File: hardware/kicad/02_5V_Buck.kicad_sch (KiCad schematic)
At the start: 9 parts, among them U101 LMR36520ADDAR 5V/2A CANDIDATE

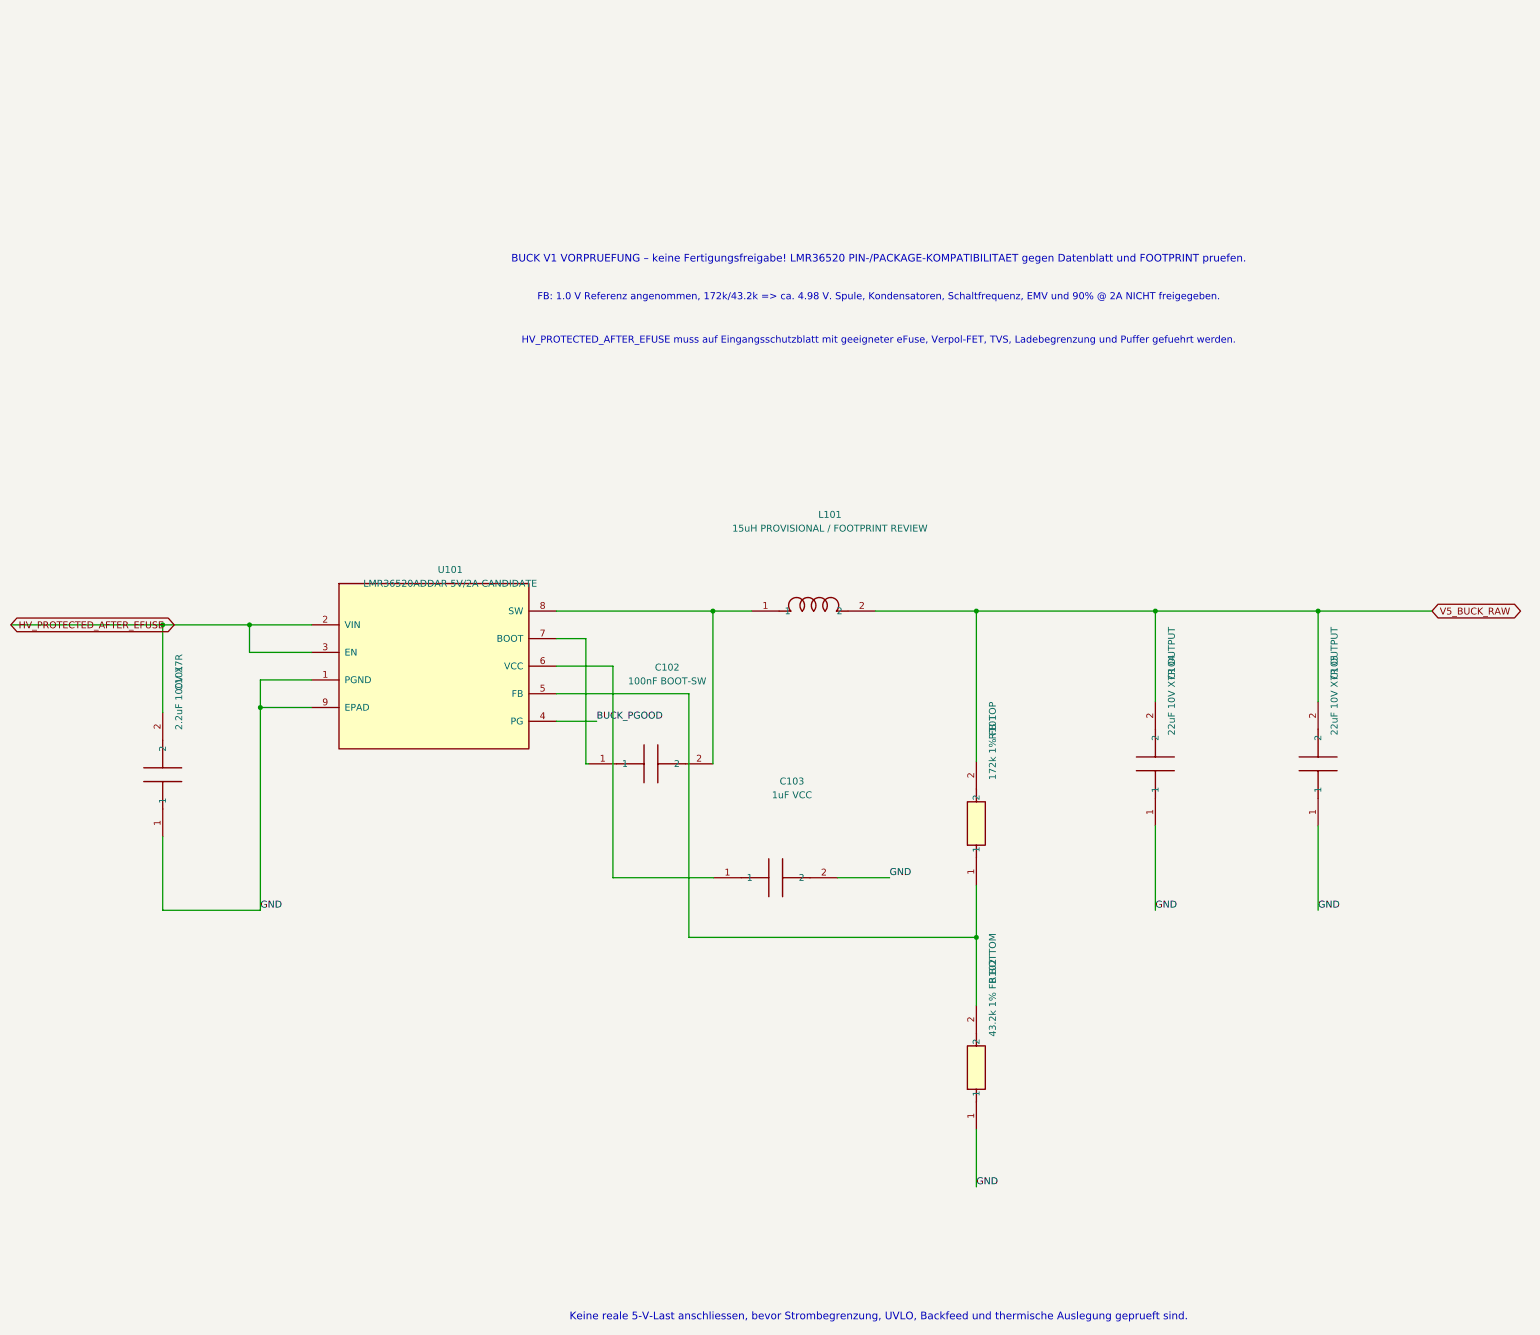
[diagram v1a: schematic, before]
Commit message: kicad: update 5V buck TI Rev C passives, 5A inductor candidate, isolate ENABLE from VIN
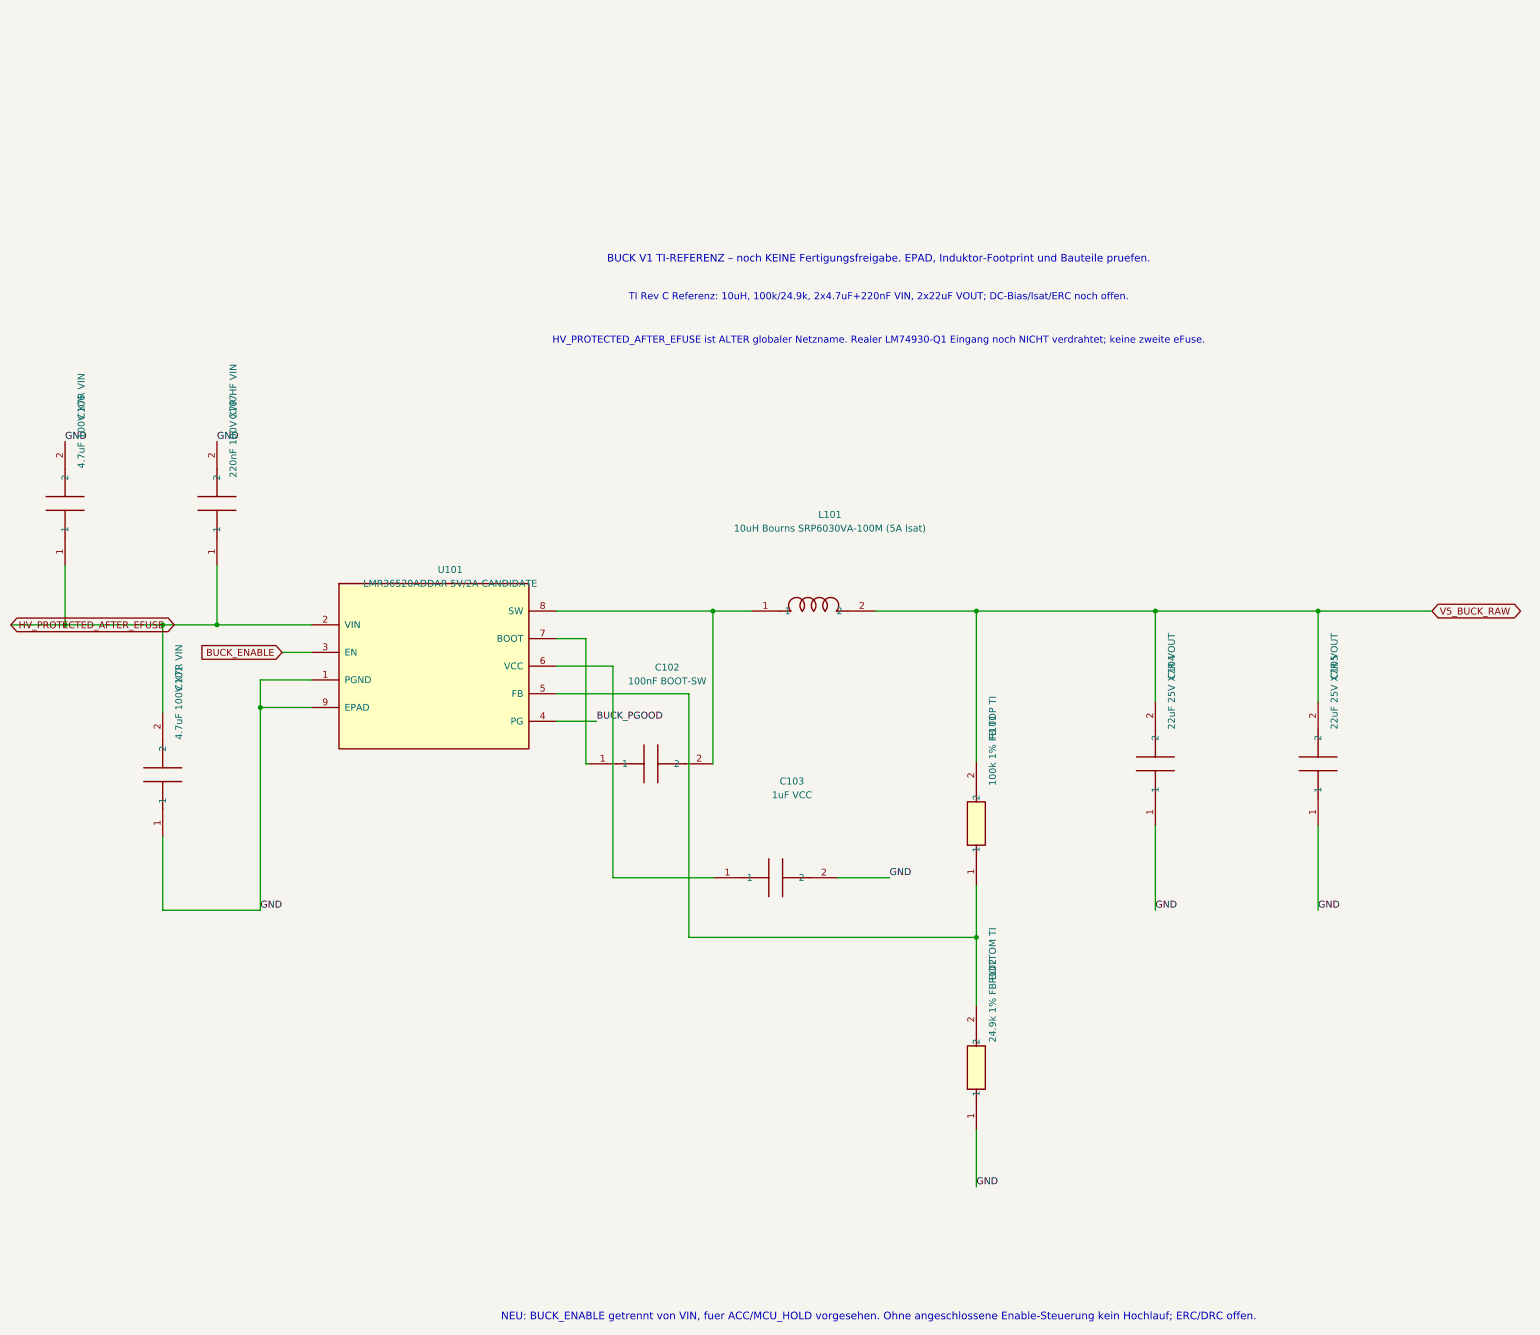
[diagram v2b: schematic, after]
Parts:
- added C106: 4.7uF 100V X7R VIN, Tripmaster:C_1210_3225, symbol Tripmaster_Sym:C1210
- added C107: 220nF 100V X7R HF VIN, Tripmaster:C_1206_3216, symbol Tripmaster_Sym:C
- C101: value 2.2uF 100V X7R -> 4.7uF 100V X7R VIN
- C104, C105: value 22uF 10V X7R OUTPUT -> 22uF 25V X7R VOUT
- L101: value 15uH PROVISIONAL / FOOTPRINT REVIEW -> 10uH Bourns SRP6030VA-100M (5A Isat); footprint Tripmaster:L1_Bourns_SRN6045_220M -> (none)
- R101: value 172k 1% FB TOP -> 100k 1% FB TOP TI
- R102: value 43.2k 1% FB BOTTOM -> 24.9k 1% FB BOTTOM TI
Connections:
- net GND: now also C106.2, C107.2
- net HV_PROTECTED_AFTER_EFUSE: now also C106.1, C107.1; no longer U101.3 (EN)
- new net BUCK_ENABLE: U101.3 (EN)
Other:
- note added: "BUCK V1 TI-REFERENZ – noch KEINE Fertigungsfreigabe. EPAD, Induktor-Footprint und Bauteile pruefen."
- note added: "HV_PROTECTED_AFTER_EFUSE ist ALTER globaler Netzname. Realer LM74930-Q1 Eingang noch NICHT verdrahtet; keine zweite eFuse."
- note added: "NEU: BUCK_ENABLE getrennt von VIN, fuer ACC/MCU_HOLD vorgesehen. Ohne angeschlossene Enable-Steuerung kein Hochlauf; ERC/DRC offen."
- note added: "TI Rev C Referenz: 10uH, 100k/24.9k, 2x4.7uF+220nF VIN, 2x22uF VOUT; DC-Bias/Isat/ERC noch offen."
- note removed: "BUCK V1 VORPRUEFUNG – keine Fertigungsfreigabe! LMR36520 PIN-/PACKAGE-KOMPATIBILITAET gegen Datenblatt und FOOTPRINT pruefen."
- note removed: "FB: 1.0 V Referenz angenommen, 172k/43.2k => ca. 4.98 V. Spule, Kondensatoren, Schaltfrequenz, EMV und 90% @ 2A NICHT freigegeben."
- note removed: "HV_PROTECTED_AFTER_EFUSE muss auf Eingangsschutzblatt mit geeigneter eFuse, Verpol-FET, TVS, Ladebegrenzung und Puffer gefuehrt werden."
- note removed: "Keine reale 5-V-Last anschliessen, bevor Strombegrenzung, UVLO, Backfeed und thermische Auslegung geprueft sind."
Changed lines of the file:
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@@
 (kicad_sch (version 20250114) (generator "eeschema")
- (paper "A3") (title_block (title "TripTracer V1 – 5 V Buck: ELEKTRISCHER ENTWURF") (date "2026-10-13") (rev "a0 / ERC NICHT GEPRUEFT"))
- (text "BUCK V1 VORPRUEFUNG – keine Fertigungsfreigabe! LMR36520 PIN-/PACKAGE-KOMPATIBILITAET gegen Datenblatt und FOOTPRINT pruefen." (at 200 25 0) (effects (font (size 1.4 1.4))))
- (text "FB: 1.0 V Referenz angenommen, 172k/43.2k => ca. 4.98 V. Spule, Kondensatoren, Schaltfrequenz, EMV und 90% @ 2A NICHT freigegeben." (at 200 32 0) (effects (font (size 1.3 1.3))))
- (text "HV_PROTECTED_AFTER_EFUSE muss auf Eingangsschutzblatt mit geeigneter eFuse, Verpol-FET, TVS, Ladebegrenzung und Puffer gefuehrt werden." (at 200 40 0) (effects (font (size 1.3 1.3))))
- (text "Keine reale 5-V-Last anschliessen, bevor Strombegrenzung, UVLO, Backfeed und thermische Auslegung geprueft sind." (at 200 220 0) (effects (font (size 1.4 1.4))))
+ (paper "A3") (title_block (title "TripTracer V1 – 5 V Buck: ELEKTRISCHER ENTWURF") (date "2026-10-13") (rev "a1 / TI-REF 5V 2A / ERC OFFEN"))
+ (text "BUCK V1 TI-REFERENZ – noch KEINE Fertigungsfreigabe. EPAD, Induktor-Footprint und Bauteile pruefen." (at 200 25 0) (effects (font (size 1.4 1.4))))
+ (text "TI Rev C Referenz: 10uH, 100k/24.9k, 2x4.7uF+220nF VIN, 2x22uF VOUT; DC-Bias/Isat/ERC noch offen." (at 200 32 0) (effects (font (size 1.3 1.3))))
+ (text "HV_PROTECTED_AFTER_EFUSE ist ALTER globaler Netzname. Realer LM74930-Q1 Eingang noch NICHT verdrahtet; keine zweite eFuse." (at 200 40 0) (effects (font (size 1.3 1.3))))
+ (text "NEU: BUCK_ENABLE getrennt von VIN, fuer ACC/MCU_HOLD vorgesehen. Ohne angeschlossene Enable-Steuerung kein Hochlauf; ERC/DRC offen." (at 200 220 0) (effects (font (size 1.4 1.4))))
  (symbol (lib_id "TripTracer_V1:LMR36520") (at 118 100 0) (unit 1) (exclude_from_sim no) (in_bom yes) (on_board yes) (dnp no)
  (property "Reference" "U101" (at 121 82.22 0) (effects (font (size 1.27 1.27))))
@@
 (symbol (lib_id "Tripmaster_Sym:L") (at 188 89.84 0) (unit 1) (exclude_from_sim no) (in_bom yes) (on_board yes) (dnp no)
  (property "Reference" "L101" (at 191 72.06 0) (effects (font (size 1.27 1.27))))
- (property "Value" "15uH PROVISIONAL / FOOTPRINT REVIEW" (at 191 74.6 0) (effects (font (size 1.27 1.27))))
- (property "Footprint" "Tripmaster:L1_Bourns_SRN6045_220M" (at 188 89.84 0) (effects (font (size 1.27 1.27)) (hide yes)))
+ (property "Value" "10uH Bourns SRP6030VA-100M (5A Isat)" (at 191 74.6 0) (effects (font (size 1.27 1.27))))
+ (property "Footprint" "" (at 188 89.84 0) (effects (font (size 1.27 1.27)) (hide yes)))
  (pin "1") (pin "2")
  (instances (project "TripTracer_V1" (path "/a26d9b0c-7f10-4e5a-a65f-000000000064/a26d9b0c-7f10-4e5a-a65f-000000000066" (reference "L101") (unit 1)))))
 (symbol (lib_id "Tripmaster_Sym:C1210") (at 68 120 90) (unit 1) (exclude_from_sim no) (in_bom yes) (on_board yes) (dnp no)
  (property "Reference" "C101" (at 71 102.22 0) (effects (font (size 1.27 1.27))))
- (property "Value" "2.2uF 100V X7R" (at 71 104.76 0) (effects (font (size 1.27 1.27))))
+ (property "Value" "4.7uF 100V X7R VIN" (at 71 104.76 0) (effects (font (size 1.27 1.27))))
  (property "Footprint" "Tripmaster:C_1210_3225" (at 68 120 0) (effects (font (size 1.27 1.27)) (hide yes)))
  (pin "1") (pin "2")
@@
 (symbol (lib_id "Tripmaster_Sym:C1210") (at 251 118 90) (unit 1) (exclude_from_sim no) (in_bom yes) (on_board yes) (dnp no)
  (property "Reference" "C104" (at 254 100.22 0) (effects (font (size 1.27 1.27))))
- (property "Value" "22uF 10V X7R OUTPUT" (at 254 102.76 0) (effects (font (size 1.27 1.27))))
+ (property "Value" "22uF 25V X7R VOUT" (at 254 102.76 0) (effects (font (size 1.27 1.27))))
  (property "Footprint" "Tripmaster:C_1210_3225" (at 251 118 0) (effects (font (size 1.27 1.27)) (hide yes)))
  (pin "1") (pin "2")
@@
 (symbol (lib_id "Tripmaster_Sym:C1210") (at 281 118 90) (unit 1) (exclude_from_sim no) (in_bom yes) (on_board yes) (dnp no)
  (property "Reference" "C105" (at 284 100.22 0) (effects (font (size 1.27 1.27))))
- (property "Value" "22uF 10V X7R OUTPUT" (at 284 102.76 0) (effects (font (size 1.27 1.27))))
+ (property "Value" "22uF 25V X7R VOUT" (at 284 102.76 0) (effects (font (size 1.27 1.27))))
  (property "Footprint" "Tripmaster:C_1210_3225" (at 281 118 0) (effects (font (size 1.27 1.27)) (hide yes)))
  (pin "1") (pin "2")
@@
 (symbol (lib_id "Tripmaster_Sym:R") (at 218 129 90) (unit 1) (exclude_from_sim no) (in_bom yes) (on_board yes) (dnp no)
  (property "Reference" "R101" (at 221 111.22 0) (effects (font (size 1.27 1.27))))
- (property "Value" "172k 1% FB TOP" (at 221 113.76 0) (effects (font (size 1.27 1.27))))
+ (property "Value" "100k 1% FB TOP TI" (at 221 113.76 0) (effects (font (size 1.27 1.27))))
  (property "Footprint" "Tripmaster:R_1206_3216" (at 218 129 0) (effects (font (size 1.27 1.27)) (hide yes)))
  (pin "1") (pin "2")
@@
 (symbol (lib_id "Tripmaster_Sym:R") (at 218 174 90) (unit 1) (exclude_from_sim no) (in_bom yes) (on_board yes) (dnp no)
  (property "Reference" "R102" (at 221 156.22 0) (effects (font (size 1.27 1.27))))
- (property "Value" "43.2k 1% FB BOTTOM" (at 221 158.76 0) (effects (font (size 1.27 1.27))))
+ (property "Value" "24.9k 1% FB BOTTOM TI" (at 221 158.76 0) (effects (font (size 1.27 1.27))))
  (property "Footprint" "Tripmaster:R_1206_3216" (at 218 174 0) (effects (font (size 1.27 1.27)) (hide yes)))
  (pin "1") (pin "2")
@@
 (wire (pts (xy 40 92.38) (xy 95.42 92.38)) (stroke (width 0) (type default)))
 (global_label "HV_PROTECTED_AFTER_EFUSE" (shape bidirectional) (at 40 92.38 0) (fields_autoplaced) (effects (font (size 1.27 1.27)) (justify left)))
-(wire (pts (xy 84 92.38) (xy 84 97.46)) (stroke (width 0) (type default)))
-(wire (pts (xy 84 97.46) (xy 95.42 97.46)) (stroke (width 0) (type default)))
 (wire (pts (xy 68 92.38) (xy 68 108.57)) (stroke (width 0) (type default)))
 (wire (pts (xy 68 131.43) (xy 68 145)) (stroke (width 0) (type default)))
@@
 (wire (pts (xy 140.58 110.16) (xy 148 110.16)) (stroke (width 0) (type default)))
 (label "BUCK_PGOOD" (at 148 110.16 0) (effects (font (size 1.27 1.27)) (justify left bottom)))
- (junction (at 84 92.38) (diameter 0) (color 0 0 0 0))
 (junction (at 68 92.38) (diameter 0) (color 0 0 0 0))
 (junction (at 86 107.62) (diameter 0) (color 0 0 0 0))
@@
  (sheet_instances (path "/" (page "3")))
  (embedded_fonts no)
+ (symbol (lib_id "Tripmaster_Sym:C1210") (at 50 70 90) (unit 1) (exclude_from_sim no) (in_bom yes) (on_board yes) (dnp no)
+ (property "Reference" "C106" (at 53 52.22 0) (effects (font (size 1.27 1.27))))
+ (property "Value" "4.7uF 100V X7R VIN" (at 53 54.76 0) (effects (font (size 1.27 1.27))))
+ (property "Footprint" "Tripmaster:C_1210_3225" (at 50 70 0) (effects (font (size 1.27 1.27)) (hide yes)))
+ (pin "1") (pin "2")
+ (instances (project "TripTracer_V1" (path "/a26d9b0c-7f10-4e5a-a65f-000000000064/a26d9b0c-7f10-4e5a-a65f-000000000066" (reference "C106") (unit 1)))))
+ (symbol (lib_id "Tripmaster_Sym:C") (at 78 70 90) (unit 1) (exclude_from_sim no) (in_bom yes) (on_board yes) (dnp no)
+ (property "Reference" "C107" (at 81 52.22 0) (effects (font (size 1.27 1.27))))
+ (property "Value" "220nF 100V X7R HF VIN" (at 81 54.76 0) (effects (font (size 1.27 1.27))))
+ (property "Footprint" "Tripmaster:C_1206_3216" (at 78 70 0) (effects (font (size 1.27 1.27)) (hide yes)))
+ (pin "1") (pin "2")
+ (instances (project "TripTracer_V1" (path "/a26d9b0c-7f10-4e5a-a65f-000000000064/a26d9b0c-7f10-4e5a-a65f-000000000066" (reference "C107") (unit 1)))))
+ (wire (pts (xy 90 97.46) (xy 95.42 97.46)) (stroke (width 0) (type default)))
+ (global_label "BUCK_ENABLE" (shape input) (at 90 97.46 180) (fields_autoplaced) (effects (font (size 1.27 1.27)) (justify right)))
+ (wire (pts (xy 50 81.43) (xy 50 92.38)) (stroke (width 0) (type default)))
+ (label "GND" (at 50 58.57 0) (effects (font (size 1.27 1.27)) (justify left bottom)))
+ (junction (at 50 92.38) (diameter 0) (color 0 0 0 0))
+ (wire (pts (xy 78 81.43) (xy 78 92.38)) (stroke (width 0) (type default)))
+ (label "GND" (at 78 58.57 0) (effects (font (size 1.27 1.27)) (justify left bottom)))
+ (junction (at 78 92.38) (diameter 0) (color 0 0 0 0))
 )

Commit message: kicad(buck): assign matching provisional Bourns 10uH 5A inductor footprint
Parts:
- L101: footprint (none) -> Tripmaster:L_Bourns_SRP6030VA_100M
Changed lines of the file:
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@@
  (property "Reference" "L101" (at 191 72.06 0) (effects (font (size 1.27 1.27))))
  (property "Value" "10uH Bourns SRP6030VA-100M (5A Isat)" (at 191 74.6 0) (effects (font (size 1.27 1.27))))
- (property "Footprint" "" (at 188 89.84 0) (effects (font (size 1.27 1.27)) (hide yes)))
+ (property "Footprint" "Tripmaster:L_Bourns_SRP6030VA_100M" (at 188 89.84 0) (effects (font (size 1.27 1.27)) (hide yes)))
  (pin "1") (pin "2")
  (instances (project "TripTracer_V1" (path "/a26d9b0c-7f10-4e5a-a65f-000000000064/a26d9b0c-7f10-4e5a-a65f-000000000066" (reference "L101") (unit 1)))))
